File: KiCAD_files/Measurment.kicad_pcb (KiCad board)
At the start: 2 copper layers, 90 x 63 mm, 69 parts, among them J1 Board outline, J2 Measurment_stage_outline_sign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, J3 Conn_01x02, U1 NMA1505SC, U2 AMC1100, U3 AMC1100, U4 AMC1311, U5 R-78C5.0-1.0, U6 AMS1117-3.3, U7 NMA1505SC

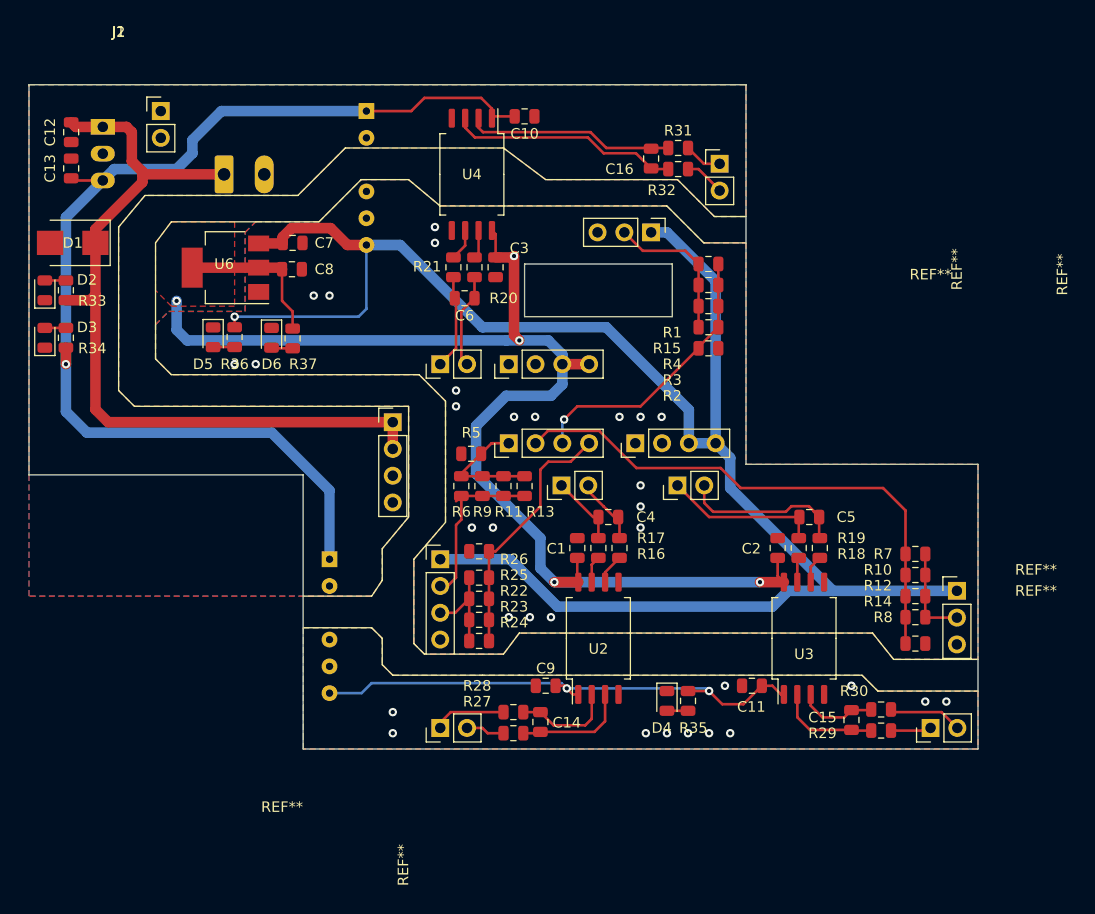
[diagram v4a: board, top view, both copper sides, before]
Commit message: Addded missing values and datasheet to measurment schematic Minor schematic modifications - added zener diodes
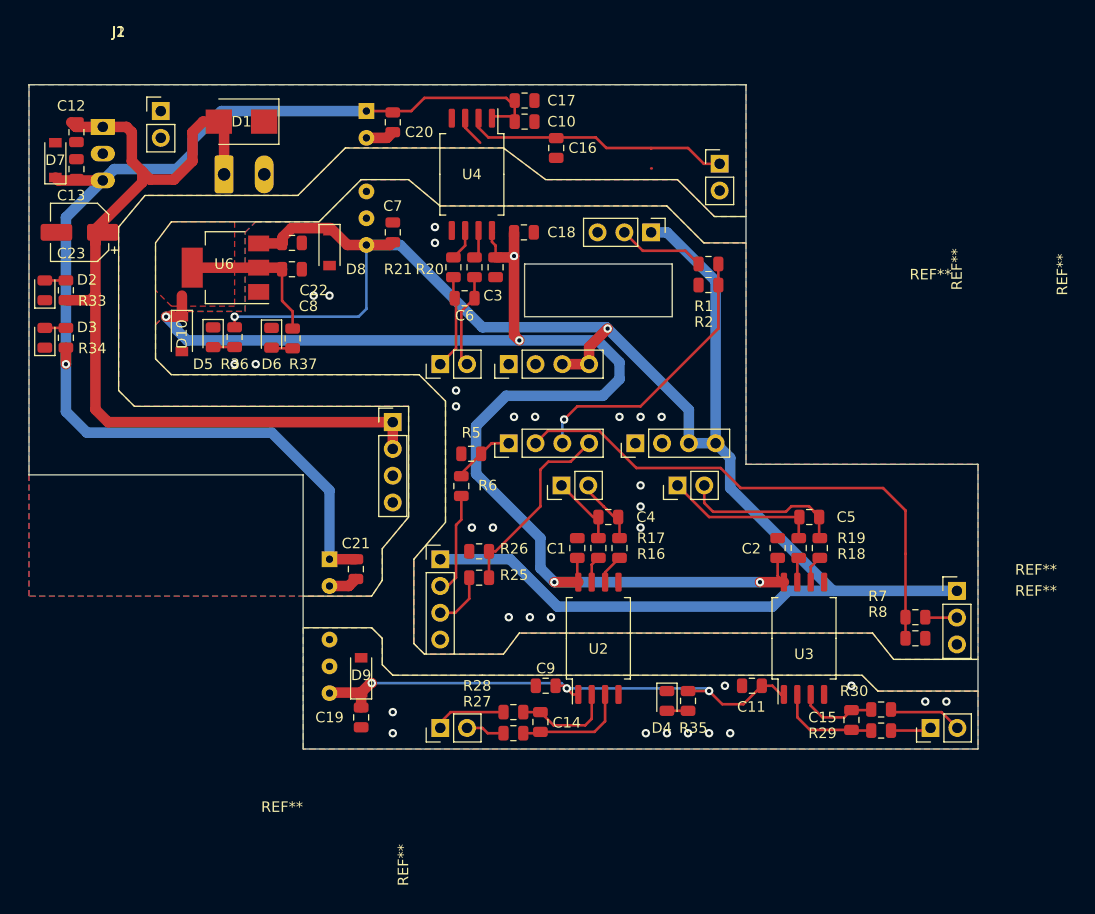
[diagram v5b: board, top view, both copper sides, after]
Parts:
- removed R10, R11, R12, R13, R14, R15, R22, R23, R24, R3, R31, R32, R4, R9: R_Small, Resistor_SMD:R_0805_2012Metric
- added C17: 1uF, Capacitor_SMD:C_0805_2012Metric, F.Cu at (78.5, 43.0)
- added C18: 1uF, Capacitor_SMD:C_0805_2012Metric, F.Cu at (78.4, 55.5)
- added C19: C_Small, Capacitor_SMD:C_0805_2012Metric, F.Cu at (63.0, 101.5)
- added C20: C_Small, Capacitor_SMD:C_0805_2012Metric, F.Cu at (66.0, 45.1)
- added C21: C_Small, Capacitor_SMD:C_0805_2012Metric, F.Cu at (62.5, 87.4)
- added C22: C_Small, Capacitor_SMD:C_0805_2012Metric, F.Cu at (56.4, 56.5)
- added C23: CP1_Small, Capacitor_SMD:CP_Elec_5x5.9, F.Cu at (36.3, 55.5)
- added D10: MMSZ5227BT1G, Diode_SMD:D_SOD-123, F.Cu at (46.0, 65.2)
- added D7: MMSZ4690T1G, Diode_SMD:D_SOD-123, F.Cu at (34.0, 48.6)
- added D8: MMSZ4690T1G, Diode_SMD:D_SOD-123, F.Cu at (60.0, 57.0)
- added D9: MMSZ4690T1G, Diode_SMD:D_SOD-123, F.Cu at (63.0, 97.5)
- C1, C10, C11, C2, C3, C9: value C_Small -> 100nF
- C14, C15, C16, C4, C5, C6: value C_Small -> 330pF
- J1: value Board outline -> Measurment_stage_outline_outputs
- R1, R25, R6, R7: value R_Small -> 20k
- R16, R17, R18, R19, R20, R21, R27, R28, R29, R30: value R_Small -> 12
- R2, R26, R5, R8: value R_Small -> 39k
- moved D1 19.7 mm to (51.6, 45.0)
- moved C7 9.55 mm to (66.0, 55.5), turned to 90 degrees
- moved C16 9.06 mm to (81.5, 47.5)
- moved R2 6.00 mm to (95.9, 60.5), turned to 180 degrees
- moved R7 6.00 mm to (115.6, 92.0)
- moved C13 0.50 mm to (36.0, 49.5)
- moved C10 0.50 mm to (78.5, 45.0)
- moved C12 0.50 mm to (36.0, 46.0)
- moved R8 0.50 mm to (115.6, 94.0)
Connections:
- C16 pad 1: Net-(C16-Pad1) -> /VIHigh+
- D1 pad 1: +15V -> GNDREF
- D1 pad 2: GNDREF -> +15V
- J1 pad 13: +3V3 -> +5VD
- J2 pad 11: /VIHigh- -> GNDREF
- U4 pad 2: Net-(C16-Pad1) -> /VIHigh+
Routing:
- net /VIHigh+: track 3.62 -> 25.2 mm
- net Net-(C16-Pad1): track 19.7 -> 0.00 mm
- net GNDREF: track 21.8 -> 8.52 mm
- net +3V3: track 129.6 -> 142.1 mm
- net +5VD: track 168.2 -> 177.4 mm, vias 1 -> 2
- net +15V: track 76.9 -> 85.6 mm
- net /IILow1: track 16.5 -> 9.78 mm
- net +5V: track 107.1 -> 113.5 mm
- net /IILow1_ADC: track 11.9 -> 5.94 mm
- net /VTh_ADC: track 24.3 -> 18.3 mm
- net /IILow2: track 9.02 -> 3.02 mm
- net /IIHigh: track 14.3 -> 8.28 mm
- net /VTh: track 9.48 -> 5.30 mm
- net /VIHigh-: track 3.87 -> 0.00 mm
- net +5P: track 49.9 -> 51.3 mm, vias 2 -> 3

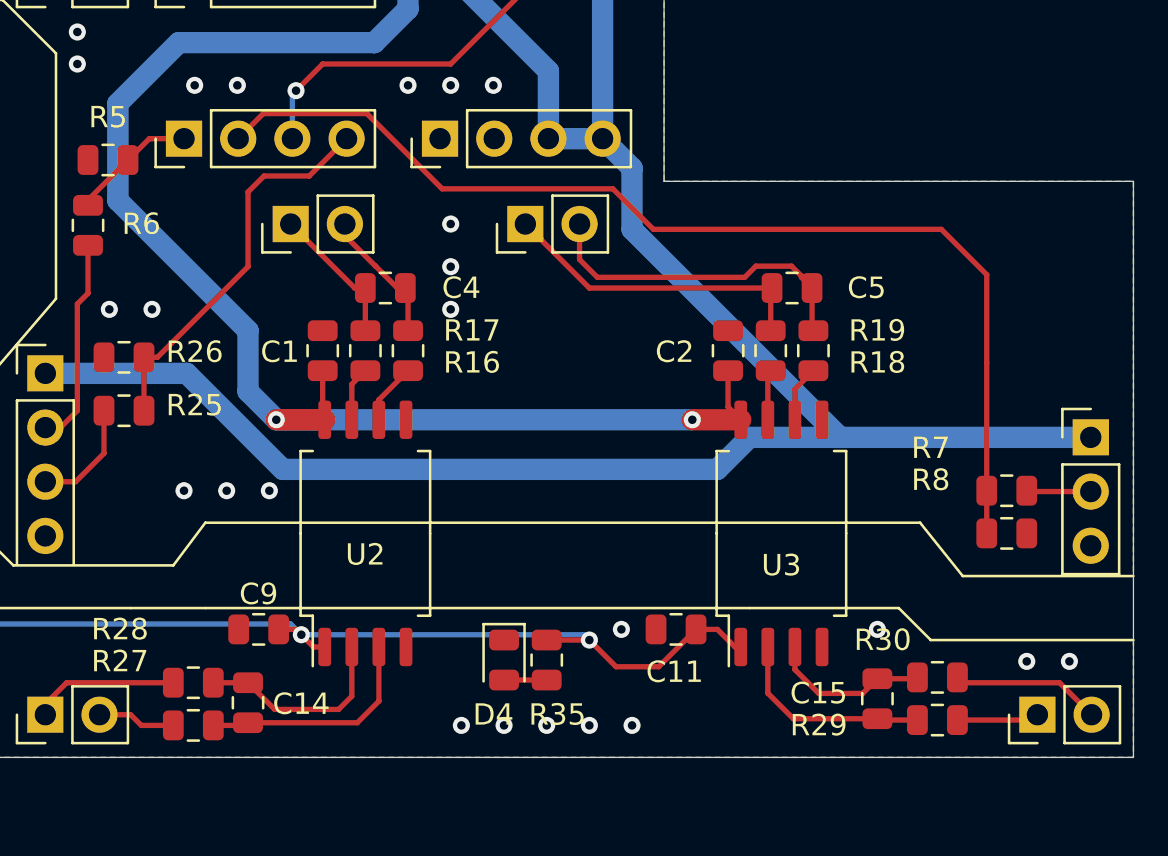
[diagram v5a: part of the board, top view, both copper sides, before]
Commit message: Added BOM files
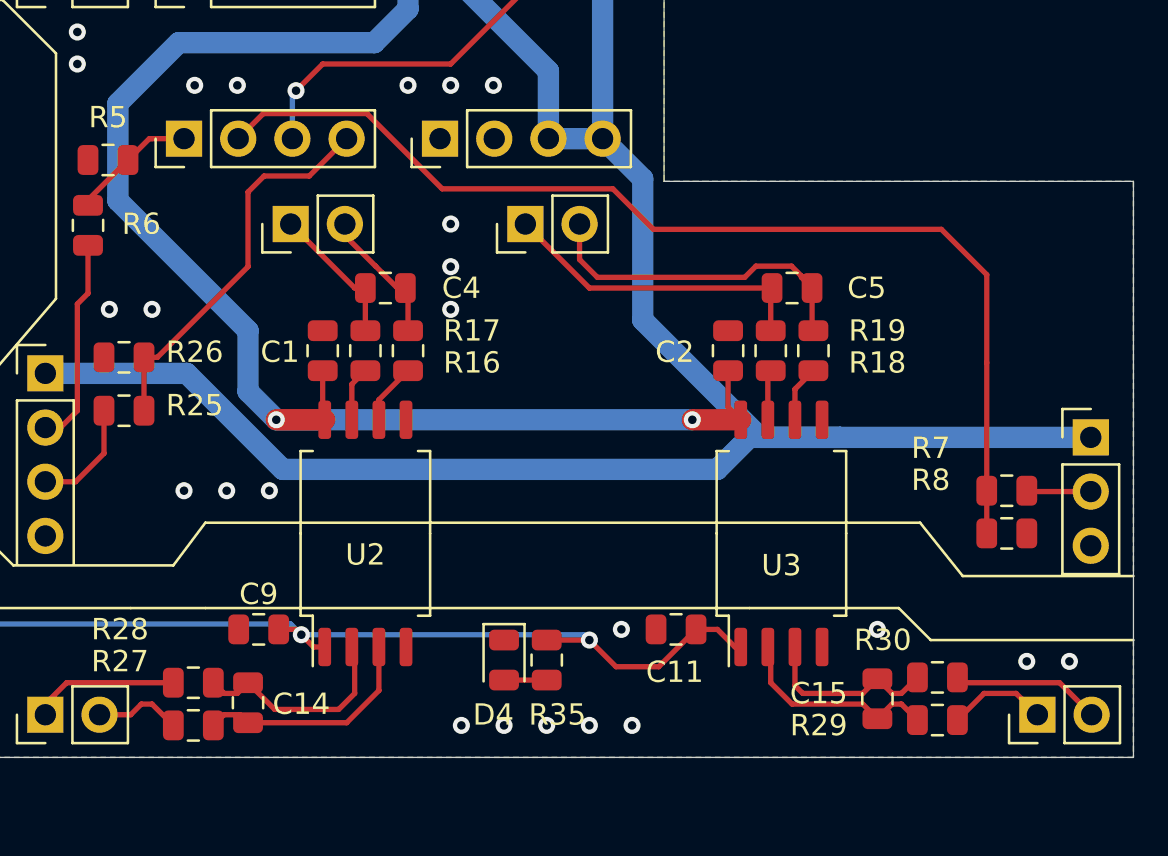
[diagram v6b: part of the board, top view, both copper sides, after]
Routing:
- net +5VD: track 177.4 -> 179.6 mm
- net Net-(C15-Pad2): track 7.57 -> 8.58 mm
- net /VILow2+: track 3.85 -> 4.68 mm
- net Net-(C14-Pad1): track 9.57 -> 10.1 mm

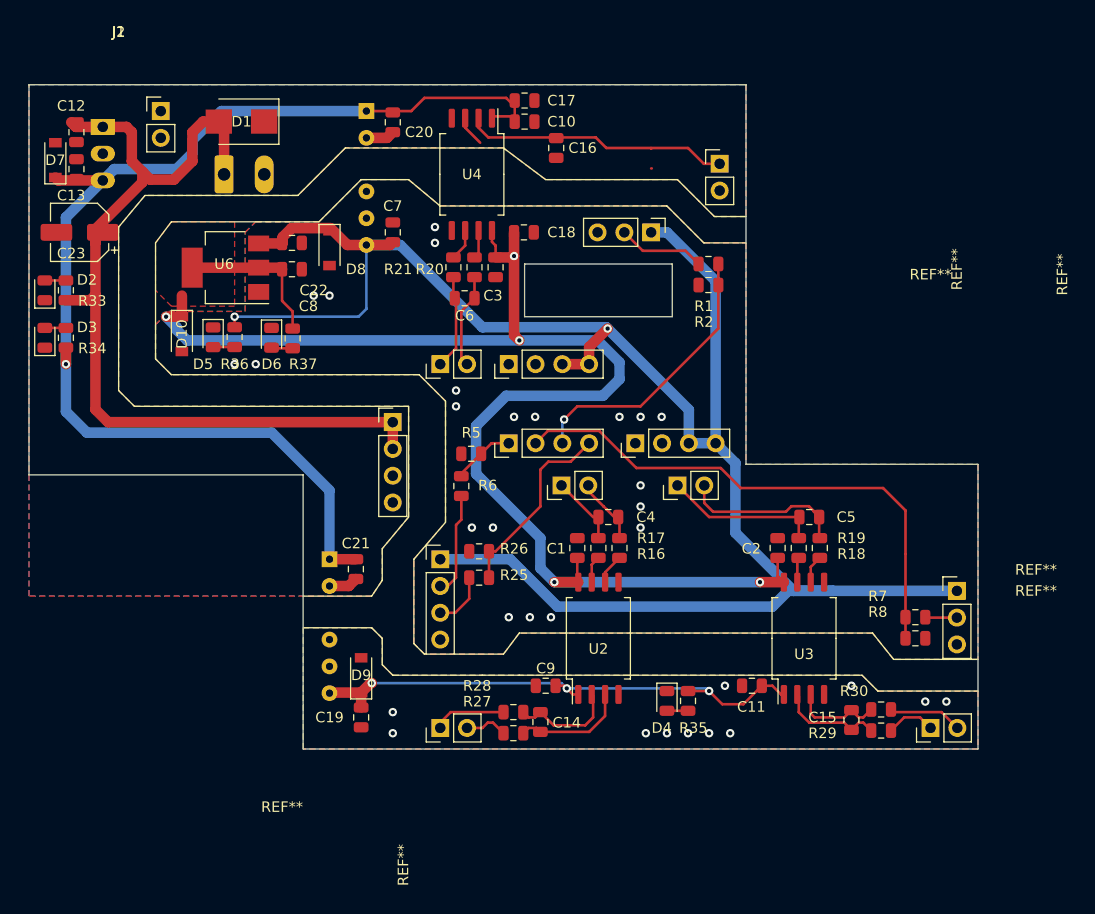
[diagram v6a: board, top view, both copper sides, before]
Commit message: Finalized BOM - Added mezzanine connectors overlay - Improved Nucleo shield
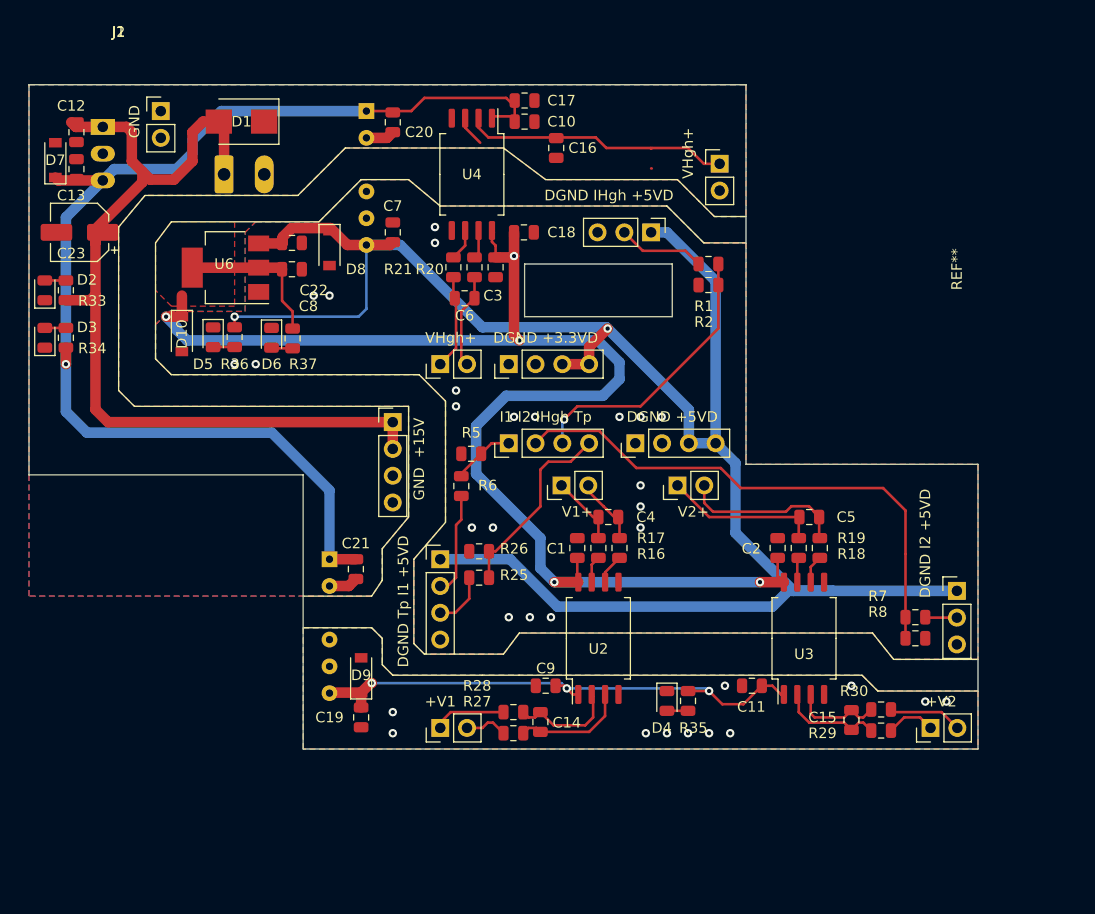
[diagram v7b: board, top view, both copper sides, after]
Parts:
- J1: value Measurment_stage_outline_outputs -> Board outline

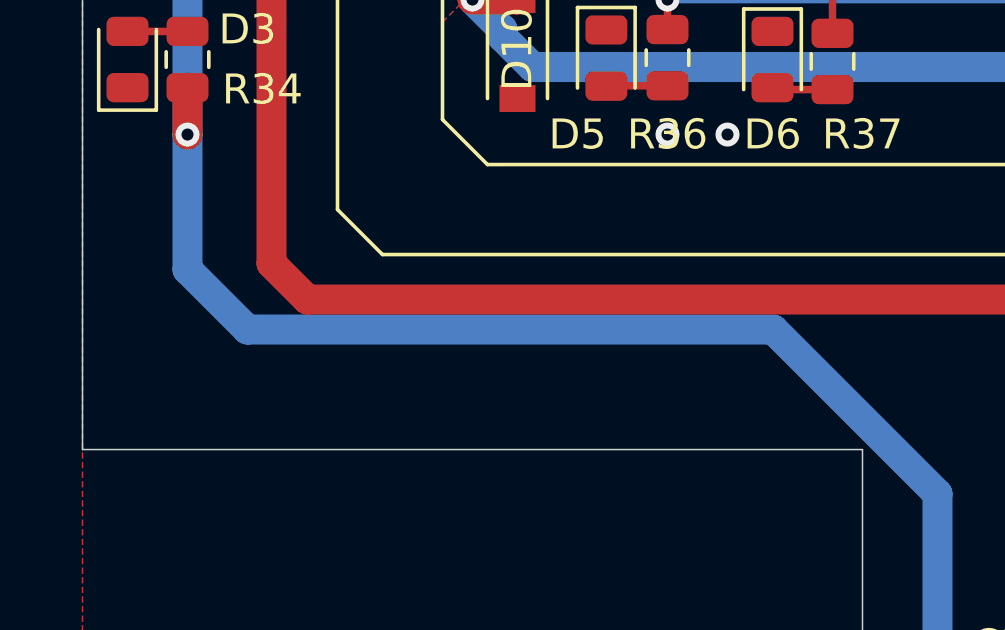
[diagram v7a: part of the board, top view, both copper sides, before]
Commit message: Finalized overlay and added License info and current version Finalized the nucleo shield - added a CR2032 battery holder for the RTC.
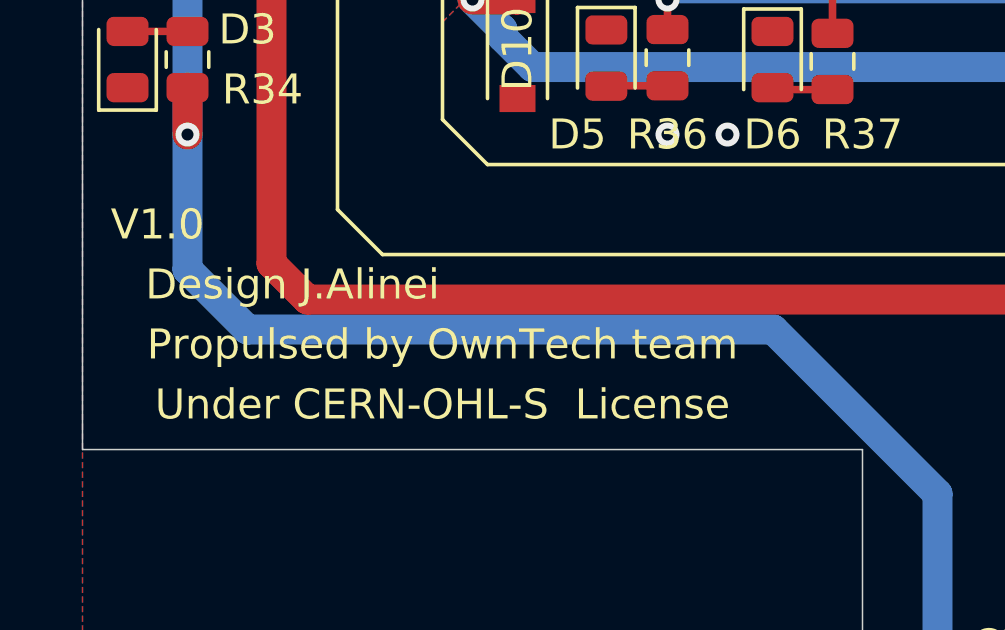
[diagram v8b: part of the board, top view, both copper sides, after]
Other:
- board text added: "Design J.Alinei"
- board text added: "Propulsed by OwnTech team"
- board text added: "Under CERN-OHL-S License"
- board text added: "V1.0"
